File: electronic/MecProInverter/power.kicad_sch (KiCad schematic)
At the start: 0 parts

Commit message: electronic
- power: added 3.3V coverter
- power: added bridge rectifier
- power: added half bridge
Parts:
- added C1, C10, C11, C12, C13, C15, C16, C19, C2, C21, C22, C24, C25, C26, C3, C4, C5, C6, C8, C9: C, symbol Device:C
- added C14, C17, C18, C20, C7: C_Polarized, symbol Device:C_Polarized
- added L1: L, symbol Device:L
- added R1, R10, R11, R12, R2, R3, R4, R5, R6, R7, R8, R9: R, symbol Device:R
- added U3: IKCM20L60GA, footprint:DIP-24_L36.0-W21.0-P1.60-LS28.6-TL, symbol IKCM20L60GA:IKCM20L60GA
- added U4: LVE2560E, symbol LVE2560E:LVE2560E
- added U5: TPS563201DDCR, footprint:SOT-23-6_L2.9-W1.6-P0.95-LS2.8-BL, symbol TPS563201DDCR:TPS563201DDCR
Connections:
- new net: C16.2, C17.1, U3.1 (VS(U))
- new net: C16.1, C17.2, U3.2 (VB(U))
- new net: R4.1, U3.17 (NW)
- new net: C14.2, C15.1, U3.4 (VB(V))
- new net: C14.1, C15.2, U3.3 (VS(V))
- new net: C18.1, C19.2, U3.5 (VS(W))
- new net: C18.2, C19.1, U3.6 (VB(W))
- new net: L1.2, U5.2 (SW)
- new net: R11.1, R12.1, U5.4 (VFB)
- new net: C24.2, U5.6 (VBST)
- new net: C11.1, R7.1, U3.9 (HIN(W))
- new net: C1.1, C2.1, C3.1, C4.1, C5.1, C7.1, U3.23 (P), U4.1 (VDD)
- new net: R1.2, U4.2 (~Phase)
- new net: C9.1, R9.1, U3.11 (LIN(V))
- new net: C12.1, R6.1, U3.8 (HIN(V))
- new net: R3.1, U3.18 (NV)
- new net: C8.1, R10.1, U3.12 (LIN(W))
- new net: C10.1, R8.1, U3.10 (LIN(U))
- new net: R2.1, U3.19 (NU)
- new net: C13.1, R5.1, U3.7 (HIN(U))
- new net +15V: C20.1, C6.1, U3.13 (VDD)
- new net +3.3V: C24.1, C25.1, C26.1, L1.1, R11.2
- new net GND: C1.2, C10.2, C11.2, C12.2, C13.2, C2.2, C20.2, C21.2, C22.2, C25.2, C26.2, C3.2, C4.2, C5.2, C6.2, C7.2, C8.2, C9.2, R12.2, R2.2, R3.2, R4.2, U3.16 (VSS), U4.4 (GND)
- new net VS: C21.1, C22.1, U5.3 (VIN), U5.5 (EN)
- no-connect marks 0 -> 1

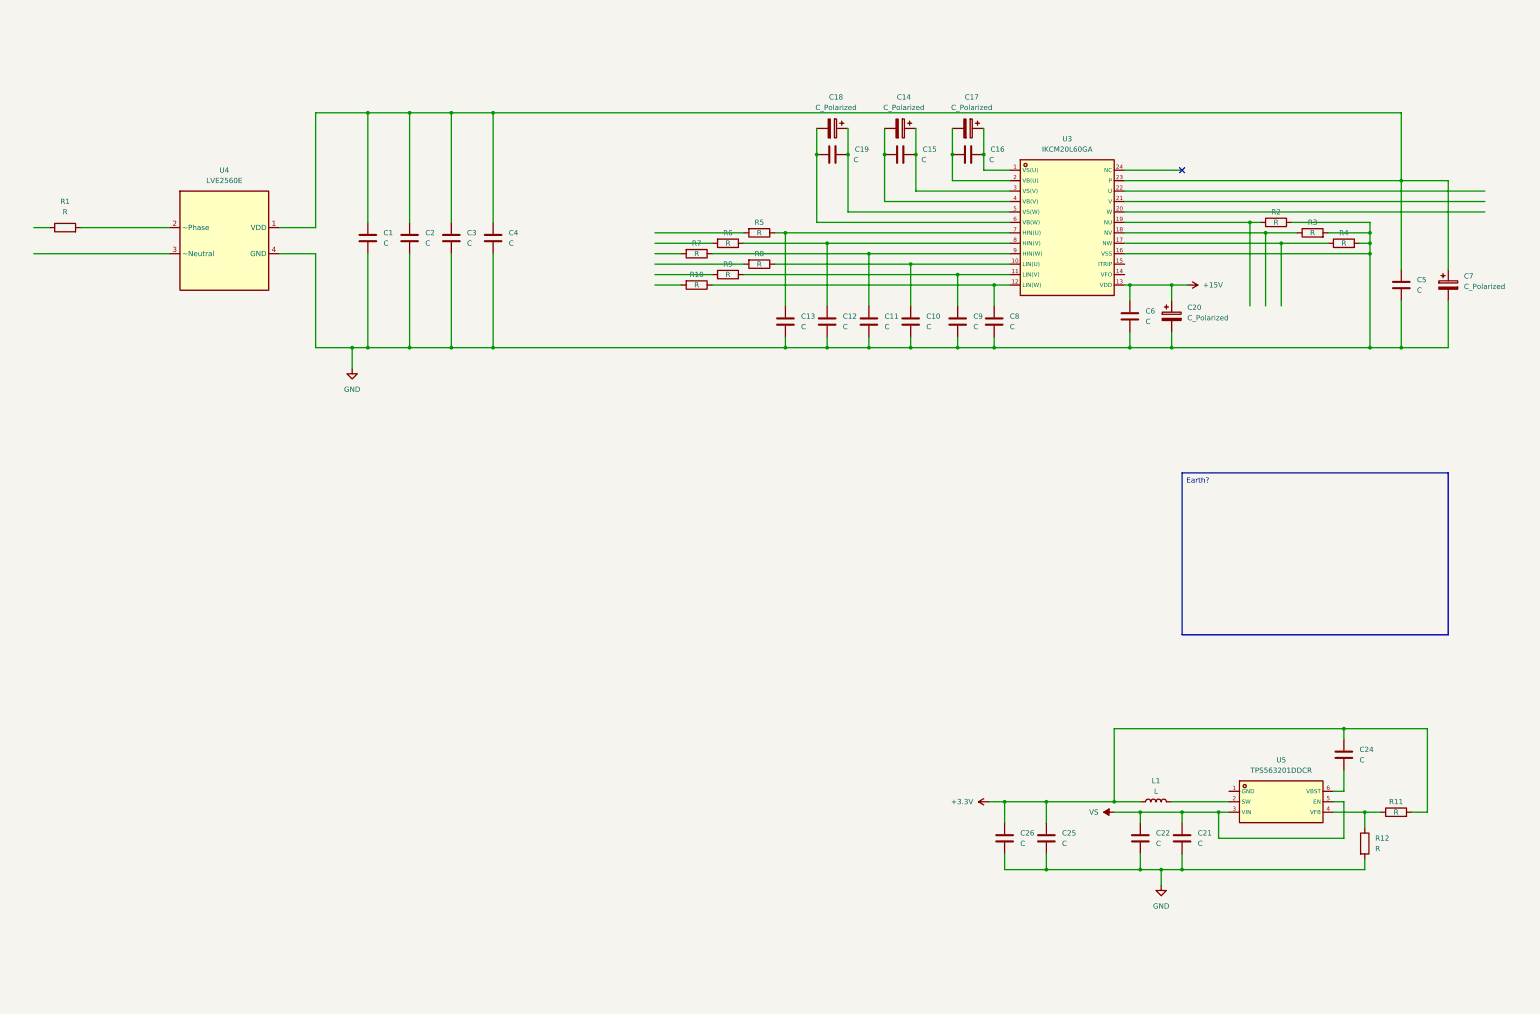
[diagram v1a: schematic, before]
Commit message: electronic
-power: added 15/3,3 Volt voltage regulator
- power: added power relay
- control: added USB-ISO, added User interface
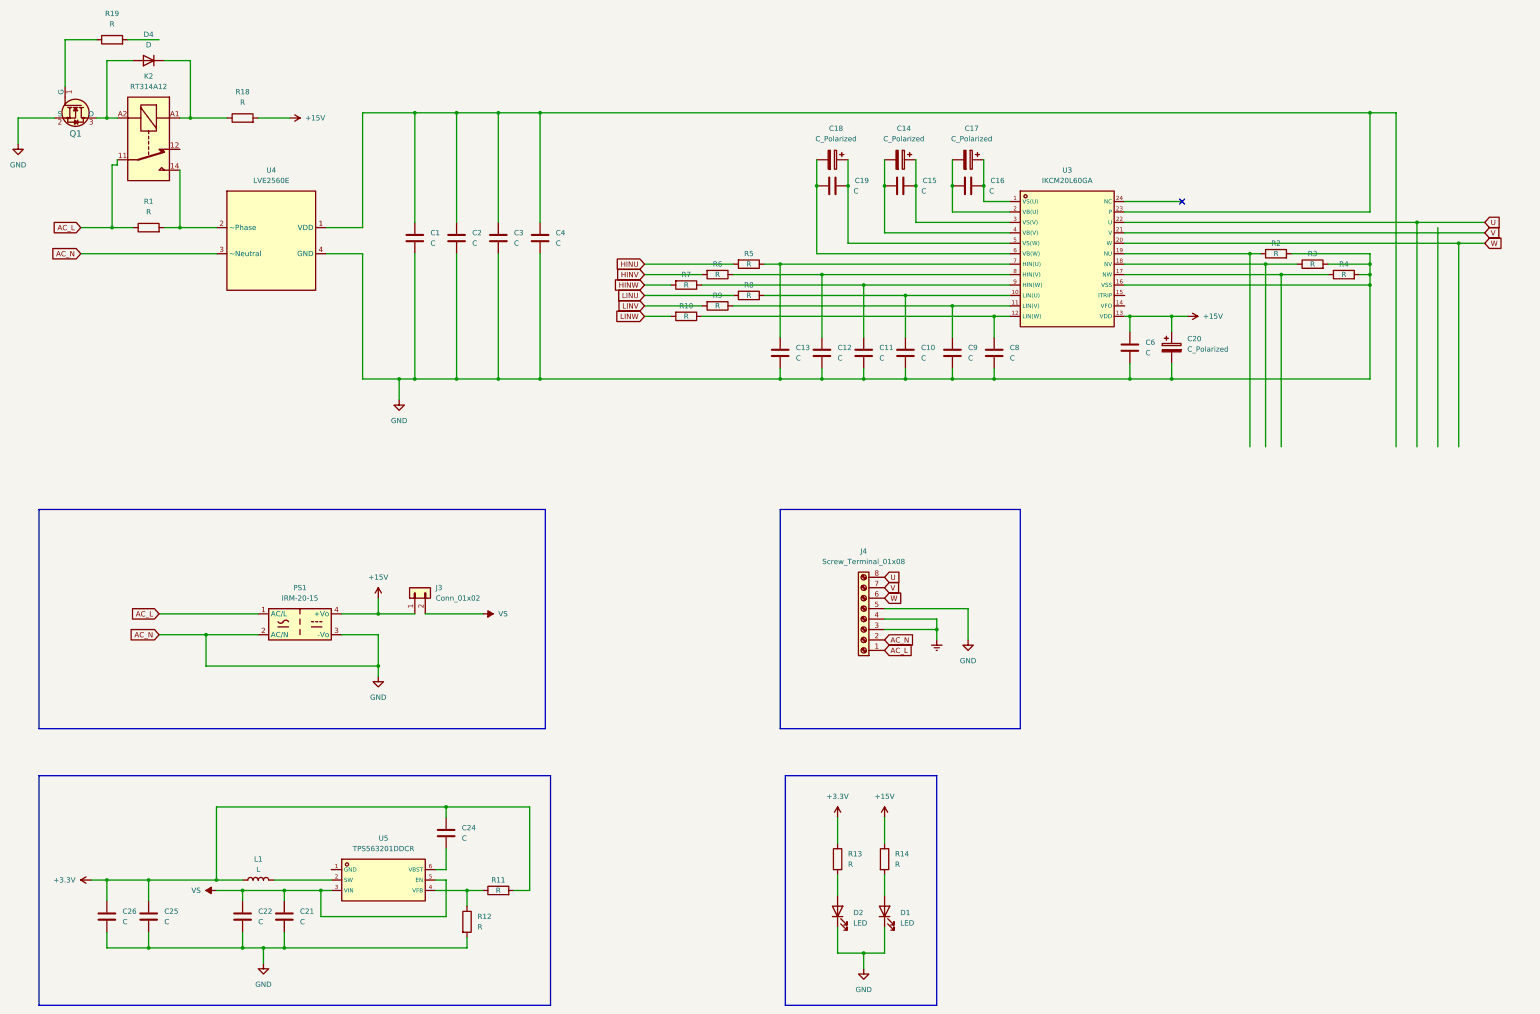
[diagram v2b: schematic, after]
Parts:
- removed C5: C, symbol Device:C
- removed C7: C_Polarized, symbol Device:C_Polarized
- added D1, D2: LED, symbol Device:LED
- added D4: D, symbol Device:D
- added J3: Conn_01x02, symbol Connector_Generic:Conn_01x02
- added J4: Screw_Terminal_01x08, symbol Connector:Screw_Terminal_01x08
- added K2: RT314A12, Relay_THT:Relay_SPDT_Schrack-RT1-16A-FormC_RM5mm, symbol Relay:RT314A12
- added PS1: IRM-20-15, Converter_ACDC:Converter_ACDC_MeanWell_IRM-20-xx_THT, symbol Converter_ACDC:IRM-20-15
- added Q1: IRLML2402TRPBF, digikey-footprints:SOT-23-3, symbol dk_Transistors-FETs-MOSFETs-Single:IRLML2402TRPBF
- added R13, R14, R18, R19: R, symbol Device:R
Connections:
- net +15V: now also J3.1 (Pin_1), PS1.4 (+Vo), R14.1, R18.2
- net +3.3V: now also R13.1
- net GND: now also U4.3 (~Neutral), D1.1 (K), D2.1 (K), J4.2 (Pin_2), J4.5 (Pin_5), PS1.2 (AC/N), PS1.3 (-Vo), Q1.2 (S)
- net VS: now also J3.2 (Pin_2)
- net at R1.2, U4.2 (~Phase): now also K2.14
- net LINV: now reaches R9.2
- net HINV: now reaches R6.2
- net AC_L: now reaches R1.1
- net AC_L: now also J4.1 (Pin_1), K2.11, PS1.1 (AC/L)
- net W: now reaches U3.20 (W)
- net W: now also J4.6 (Pin_6)
- net V: now reaches U3.21 (V)
- net V: now also J4.7 (Pin_7)
- net U: now reaches U3.22 (U)
- net U: now also J4.8 (Pin_8)
- net LINU: now reaches R8.2
- net LINW: now reaches R10.2
- net HINW: now reaches R7.2
- net HINU: now reaches R5.2
- new net: D4.1 (K), K2.A1, R18.1
- new net: D4.2 (A), K2.A2, Q1.3 (D)
- new net: Q1.1 (G), R19.1
- new net: D1.2 (A), R14.2
- new net: D2.2 (A), R13.2
- new net Earth: J4.3 (Pin_3), J4.4 (Pin_4)
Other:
- moved on the sheet: C1, C10, C11, C12, C13, C14, C15, C16, C17, C18, C19, C2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

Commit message: electronic
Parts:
- D1: value LED -> LED_15V
- D2: value LED -> LED_3.3V
- R1: value R -> 14.4
- R13: value R -> 40
- R14: value R -> 820
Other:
- moved on the sheet: D2, Q1, R13
